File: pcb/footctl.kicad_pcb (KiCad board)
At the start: 2 copper layers, 100 x 100 mm, 53 parts, among them J1 Conn_01x10_Female, J10 Conn_01x05_Female, J11 EXP2, J12 EXP1, J13 Conn_01x05_Female, J2 Conn_01x10_Female, J3 Conn_01x10_Female, J4 Conn_01x10_Female, J5 Conn_01x10_Female, J6 Conn_01x10_Female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

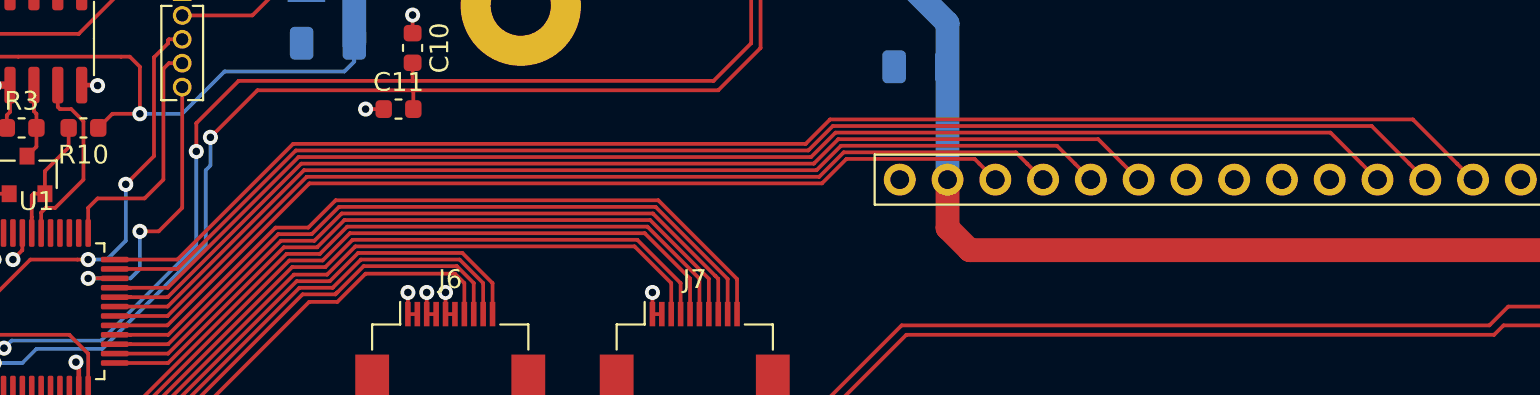
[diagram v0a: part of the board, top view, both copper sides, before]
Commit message: do not connect LCD RW pin
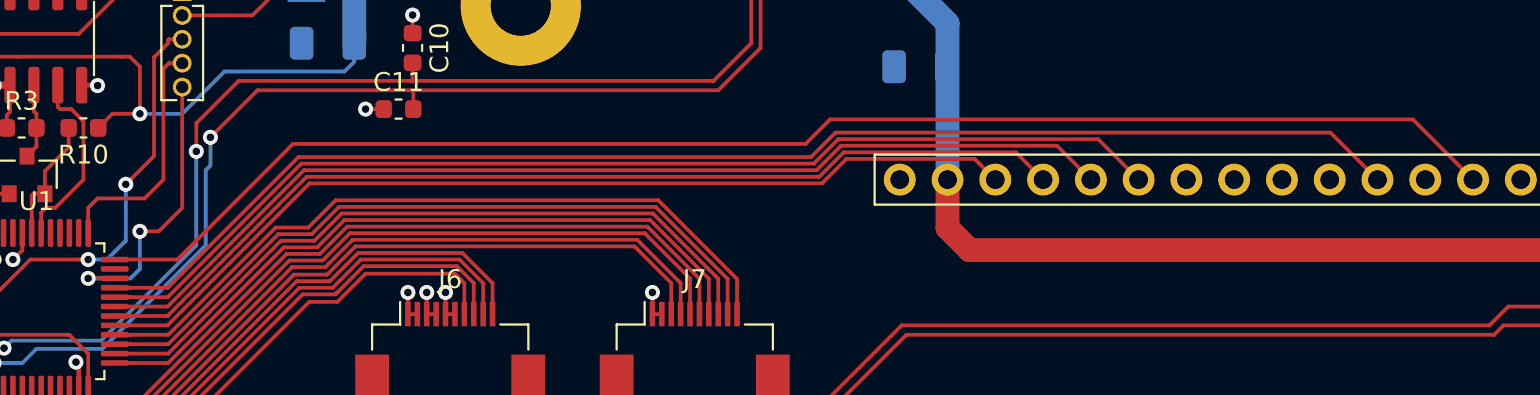
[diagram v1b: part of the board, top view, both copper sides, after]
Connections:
- DS1 pad 5: /LCDRW -> GND
- U1 pad 35: /LCDRW -> Net-(U1-Pad35)
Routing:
- net /LCDRW: track 74.0 -> 0.00 mm
